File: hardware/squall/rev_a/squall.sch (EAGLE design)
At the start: 47 parts, among them IC1 FT232RQ, J1 MICRO_USB_B_HIROSE_ZX62R-B-5P, J2 TC2030-CTX-NL, J5 MICRO_USB_B_JST_MC5BR3-M404-4S, J6 HIROSE-DF40C-10DP-0.4V, J7 HIROSE-DF40C-10DP-0.4V, U1 FT232RL, U3 NRF51822QF, U4 LDK120PU30R, X2 16MHz

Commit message: updated squall
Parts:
- removed C1, C2, C4: 0.1u, rcl:C-EUC0603
- removed C5: 10u, SparkFun:CAP_POL1206
- removed D2: BLUE, SparkFun:LED0603
- removed D3: GREEN, SparkFun:LED0603
- removed D4: RED, SparkFun:LED0603
- removed J1: MICRO_USB_B_HIROSE_ZX62R-B-5P, connector:MICRO_USB_B_HIROSE_ZX62R-B-5P
- removed L1: (no value), SparkFun:INDUCTOR0603
- removed R3, R4: 470, rcl:R-US_R0603
- removed U1: FT232RL, ftdichip:FT232RL
- R2: value 470 -> 12k; device rcl:R-US_R0603 -> passives:RESISTOR; DIGIKEY (none) -> RHM12.0KCDCT-ND
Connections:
- net N$12 renamed AVDD
- net N$13 renamed DCC
- net N$28 renamed FTDI_VCC
- removed net !RST_USB: U1.!RTS
- removed net MISO: U3.P28
- removed net MOSI: U3.P29
- removed net N$10: R2.1, U1.CBUS0
- removed net N$15: R3.1, U1.CBUS1
- removed net N$20: D2.C, R2.2
- removed net N$21: D3.C, R3.2
- removed net N$22: D4.C, R4.2
- removed net N$24: C16.1, J5.+5V, L4.1
- removed net N$25: C19.1, U4.EN, U4.IN
- removed net N$29: C18.1, IC1.3V3OUT, IC1.VCCIO
- removed net N$8: J1.D+, U1.USBDP
- removed net N$9: C2.1, C5.+, L1.2, U1.VCC
- removed net RX: U1.TXD
- removed net SCK: U3.P25
- removed net TX: U1.RXD
- removed net USB5V: C1.1, J1.+5V, L1.1
- new net 5V: C16.1, C19.1, J5.+5V, J7.10, J7.8, L4.1, U4.EN, U4.IN
- new net A5: J6.9, U3.P04/AIN5
- new net A6: J6.7, U3.P05/AIN6
- new net A7: J6.5, U3.P06/AIN7/AREF1
- new net P08: J6.3, U3.P08
- new net P09: J6.1, U3.P09
- new net P10: J6.10, U3.P10
- new net P11: J6.8, U3.P11
- new net P12: J6.6, U3.P12
- new net PROG_RX: IC1.TXD, U3.P28
- new net PROG_TX: IC1.RXD, U3.P29
- net 3V3: now also C18.1, IC1.3V3OUT, IC1.VCCIO; no longer C4.1, D2.A, D3.A, D4.A, U1.3V3OUT, U1.VCCIO
- net GND: now also BAT1.-, J7.1, J7.9, U$2.-; no longer C1.2, C2.2, C4.2, C5.-, J1.GND, R4.1, U1.GND, U1.GND@1, U1.GND@2, U1.GND@A, U1.TEST
- net N$1: now also R2.2, U$2.+; no longer J1.D-, U1.USBDM
- net N$7: now also U3.P13; no longer U3.P09
- net SWDCLK: now also J6.2
- net SWDIO: now also J6.4
- net TCK: no longer U1.!DTR
- net VCC: now also BAT1.+, J7.2, J7.4, R2.1
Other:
- moved on the sheet: BAT1, J6, J7, R2, U$2

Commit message: squall mostly routed
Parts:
- removed A3: FRACTUS-2.4GHZ-FR05-S1-N-0-110, chips:FRACTUS-2.4GHZ-FR05-S1-N-0-110
- removed C19, C20: 1uF, passives:CAPACITOR
- removed U4: LDK120PU30R, chips:LDK120PU30R
- added DDDDD: DIODE, passives:CAPACITOR
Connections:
- removed net N$31: C20.1, U4.OUT
- new net A0: J7.6, U3.P26/AIN0/XL2
- new net A1: J7.8, U3.P27/AIN1/XL1
- new net P24: J7.2, U3.P24
- new net P25: J7.4, U3.P25
- net 3V3: now also DDDDD.2
- net 5V: now also J7.5, J7.7; no longer C19.1, J7.10, J7.8, U4.EN, U4.IN
- net GND: now also J7.10; no longer C19.2, C20.2, J7.1, U4.GND
- net VCC: now also DDDDD.1, J7.1, J7.3; no longer J7.2, J7.4

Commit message: squall routed
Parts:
- removed DDDDD: DIODE, passives:CAPACITOR
- removed J2: TC2030-CTX-NL, connector:TC2030-CTX-NL
- added C1: 0.8pF, passives:CAPACITOR
- added D2: DIODE, passives:DIODE
- added J23: TC2030-JLINK-NL, connector:TC2030-JLINK-NL
- added LOGO1: UMICH_SOLID_TINY, logos:UMICH_SOLID_TINY
- R2: value 12k -> (none); DIGIKEY RHM12.0KCDCT-ND -> (none)
- renumbered IC1 to U2, U$2 to BAT2
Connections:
- removed net !RESET: J2.!RESET
- removed net TCK: J2.TCK
- removed net TDO: J2.TDO
- removed net TMS: J2.TMS
- new net P07: J6.3, U3.P07
- net 3V3: now also D2.ANODE; no longer DDDDD.2
- net GND: now also C1.2, J23.GND; no longer J2.GND
- net N$11: now also C1.1
- net P08: now also J6.1; no longer J6.3
- net P09: now also J6.10; no longer J6.1
- net P10: now also J6.8; no longer J6.10
- net P11: now also J6.6; no longer J6.8
- net P12: no longer J6.6
- net SWDCLK: now also J23.SWCLK
- net SWDIO: now also J23.SWDIO
- net VCC: now also D2.CATHODE, J23.VCC; no longer DDDDD.1, J2.VCC
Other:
- moved on the sheet: A2

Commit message: updated squall
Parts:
- removed U$1: UMICH_SOLID_SMALL, logos:UMICH_SOLID_SMALL
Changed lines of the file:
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@@
 </classes>
 <parts>
-<part name="U$1" library="logos" deviceset="UMICH_SOLID" device="_SMALL"/>
 <part name="C7" library="passives" deviceset="CAPACITOR" device="" value="0.1uF">
 <attribute name="DIGIKEY" value="445-4952-1-ND"/>
@@
 <instance part="GND12" gate="1" x="91.44" y="127"/>
 <instance part="GND13" gate="1" x="78.74" y="35.56"/>
-<instance part="U$1" gate="G$1" x="232.664" y="22.352"/>
 <instance part="U3" gate="G$1" x="78.74" y="86.36"/>
 <instance part="GND6" gate="1" x="167.64" y="48.26"/>

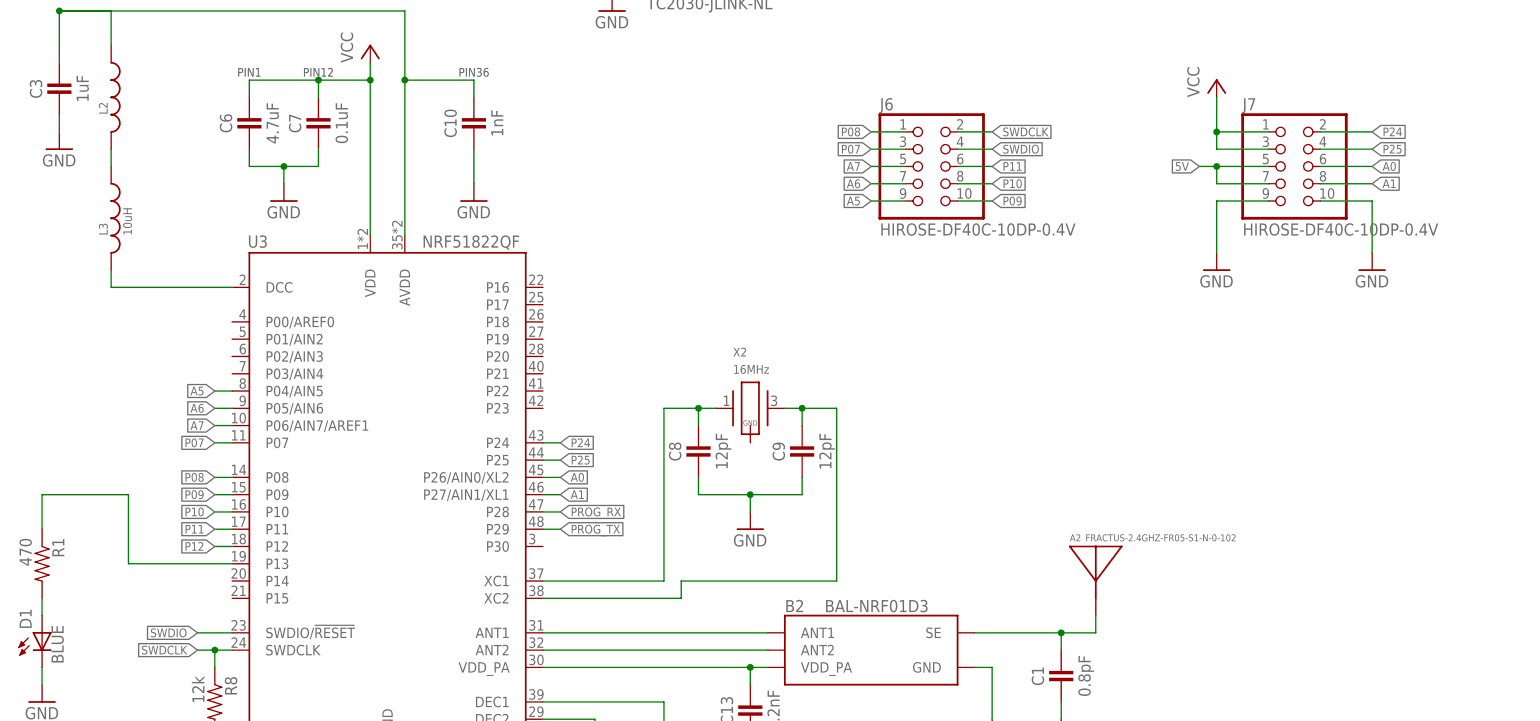
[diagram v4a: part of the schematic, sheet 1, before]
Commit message: added 32khz crystal to squall
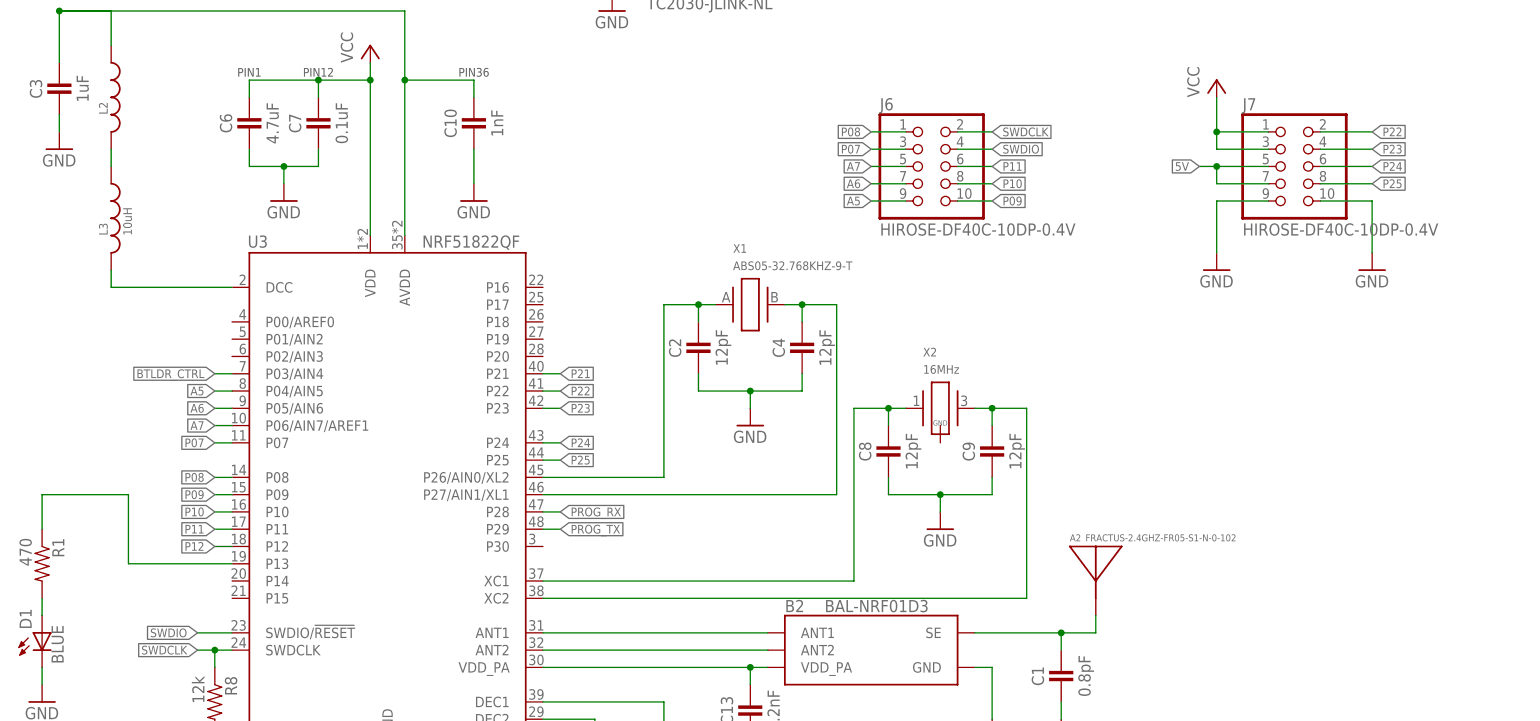
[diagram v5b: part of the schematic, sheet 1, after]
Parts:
- added C2, C4: 12pF, passives:CAPACITOR
- added X1: ABS05-32.768KHZ-9-T, crystals:ABS05-32.768KHZ-9-T
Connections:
- new net BTLDR_CTRL: U2.!DTR, U3.P03/AIN4
- new net P21: U3.P21
- new net P22: J7.2, U3.P22
- new net P23: J7.4, U3.P23
- net A0: now also C2.1, X1.1; no longer J7.6
- net A1: now also C4.1, X1.2; no longer J7.8
- net GND: now also C2.2, C4.2
- net P24: now also J7.6; no longer J7.2
- net P25: now also J7.8; no longer J7.4
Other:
- moved on the sheet: C8, C9, X2

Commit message: getting close, real close to shipping squall
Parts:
- removed C16, C17, C18: 0.1uF, passives:CAPACITOR
- removed L4: (no value), passives:INDUCTOR0402
- added C14: 1uF, passives:CAPACITOR
- added C15: 4.7uF, passives:CAPACITOR
- added C5: 12pF, passives:CAPACITOR
- added L1: 15nH, passives:INDUCTOR0402
- added R3: 1k, passives:RESISTOR
- added S1: B3U-3000P-B, switches:B3U-3000P-B
- C10: value 1nF -> 0.1uF; DIGIKEY 490-1303-1-ND -> 445-4952-1-ND
- C11: value 1nF -> 0.1uF; DIGIKEY 490-1303-1-ND -> 490-1318-6-ND
- C12: value 47nF -> 0.1uF; DIGIKEY 445-1264-1-ND -> 490-1318-6-ND
- C13: value 2.2nF -> 0.1uF; DIGIKEY 490-5419-1-ND -> 490-1318-6-ND
- C3: value 1uF -> 12pF; DIGIKEY 1276-1513-1-ND -> 490-6197-1-ND
- C6: value 4.7uF -> 1nF; DIGIKEY 445-5947-1-ND -> 490-1303-1-ND
- C7: value 0.1uF -> 1nF; DIGIKEY 445-4952-1-ND -> 490-1303-1-ND
- C8: value 12pF -> 2.2nF; DIGIKEY 490-6197-1-ND -> 490-5419-1-ND
- C9: value 12pF -> 47nF; DIGIKEY 490-6197-1-ND -> 445-1264-1-ND
- L2: value (none) -> 10uH; device passives:INDUCTOR0402 -> passives:INDUCTOR0603; DIGIKEY 587-1521-1-ND -> 490-4025-1-ND
- L3: value 10uH -> (none); device passives:INDUCTOR0603 -> passives:INDUCTOR0402; DIGIKEY 490-4025-1-ND -> 445-2979-1-ND
- R1: value 470 -> 150; DIGIKEY RHM470CECT-ND -> RHM150CDCT-ND
- R2: value (none) -> 150; DIGIKEY (none) -> RHM150CDCT-ND
- renumbered R8 to R4
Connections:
- new net N$8: R1.2, S1.P$2
- net 3V3: now also C13.1; no longer C18.1
- net 5V: now also C11.1, L3.1; no longer C16.1, L4.1
- net A1: now also C3.1; no longer C4.1
- net AVDD: now also C14.1, C7.1, L1.1; no longer C10.1, C3.1, L2.1
- net DCC: now also L2.2; no longer L3.2
- net FTDI_VCC: now also C12.1, L3.2; no longer C17.1, L4.2
- net GND: now also C14.2, C15.2, C5.2, S1.P$1; no longer C16.2, C17.2, C18.2, D1.C
- net N$14: now also L1.2, L2.1; no longer L2.2, L3.1
- net N$16: now also C4.1; no longer C8.1
- net N$17: now also C5.1; no longer C9.1
- net N$18: now also C6.1; no longer C11.1
- net N$19: now also C9.1; no longer C12.1
- net N$23: now also R3.2; no longer R1.2
- net N$7: now also D1.C; no longer R1.1
- net SWDIO: now also R1.1
- net VCC: now also C10.1, C15.1, R3.1; no longer C6.1, C7.1
- net VDD_PA: now also C8.1; no longer C13.1
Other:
- moved on the sheet: C10, C2, C3, C4, C6, C7, C8, C9, D1, J6, L2, R1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

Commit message: silkscreen
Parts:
- X1: value ABS05-32.768KHZ-9-T -> 16MHz; device crystals:ABS05-32.768KHZ-9-T -> crystals:TXC-8Y; DIGIKEY (none) -> 887-2003-1-ND
- X2: value 16MHz -> ABS05-32.768KHZ-9-T; device crystals:TXC-8Y -> crystals:ABS05-32.768KHZ-9-T; DIGIKEY 887-2003-1-ND -> (none)
- renumbered A2 to A1, B2 to B1, J23 to J4, J5 to J3, J6 to J1, J7 to J2, U3 to U1
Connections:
- net A0: now also X2.1; no longer X1.1
- net A1: now also X2.2; no longer X1.2
- net N$16: now also X1.1; no longer X2.1
- net N$17: now also X1.2; no longer X2.2

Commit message: squall rev a ready to ship
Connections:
- net 5V: now also J1.5, J1.7; no longer J2.5, J2.7
- net A5: now also J2.9; no longer J1.9
- net A6: now also J2.7; no longer J1.7
- net A7: now also J2.5; no longer J1.5
- net GND: now also J1.10, J1.9; no longer J2.10, J2.9
- net P07: now also J2.3; no longer J1.3
- net P08: now also J2.1; no longer J1.1
- net P09: now also J2.10; no longer J1.10
- net P10: now also J2.8; no longer J1.8
- net P11: now also J2.6; no longer J1.6
- net P22: now also J1.2; no longer J2.2
- net P23: now also J1.4; no longer J2.4
- net P24: now also J1.6; no longer J2.6
- net P25: now also J1.8; no longer J2.8
- net SWDCLK: now also J2.2; no longer J1.2
- net SWDIO: now also J2.4; no longer J1.4
- net VCC: now also J1.1, J1.3; no longer J2.1, J2.3
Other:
- note added: "Batteries"
- note added: "FTDI Circuit for UART Programming and Communication"
- note added: "JTAG Connection"
- note added: "Left Header"
- note added: "Note: Only one battery can be connected at a time. If BAT1 is connected, do not populate D2 or R2. If BAT2 is connected, D2 and R2 must be populated for recharging."
- note added: "Reset Switch"
- note added: "Right Header"
- moved on the sheet: J1, J2
